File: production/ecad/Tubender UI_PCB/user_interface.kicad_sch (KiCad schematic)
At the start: 17 parts, among them IC3 SN74LVC1G29DCTR, J1 640387-5, J2 1-640387-0, J3 104031-0811, J4 640387-5, U5 74HC595, U6 PEC11R-4215K-S0024

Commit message: Added Display Daughter Board PCB and start UI layout
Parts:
- added C1: 0.1u, Capacitor_SMD:C_0805_2012Metric, symbol Device:C_Small
- added J5, J6: 4-1734592-0, footprints:TE_4-1734592-0, symbol SamacSys_Parts:4-1734592-0
- IC3: footprint footprints:SOP65P780X200-28N -> footprints:DCT0008A_N
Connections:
- net +3V3: now also C1.1, J5.4, J6.4; no longer C10.2, C11.2, C18.2, IC3.4 (GND), J1.5, J2.10, J3.6 (VSS), J4.5, U5.8 (GND), U6.5 (C)
- new net +24V: J5.2, J6.2
- new net BLUE0: J5.24, J6.24
- new net BLUE1: J5.25, J6.25
- new net BLUE2: J5.26, J6.26
- new net BLUE3: J5.27, J6.27
- new net BLUE4: J5.28, J6.28
- new net DE: J5.34, J6.34
- new net GND: C1.2, C10.2, C11.2, C18.2, IC3.4 (GND), J1.5, J2.10, J3.6 (VSS), J4.5, J5.13, J5.14, J5.21, J5.22, J5.23, J5.29, J5.3, J5.36, J5.5, J5.6, J5.7, J6.13, J6.14, J6.21, J6.22, J6.23, J6.29, J6.3, J6.36, J6.5, J6.6, J6.7, U5.8 (GND), U6.5 (C)
- new net GREEN0: J5.15, J6.15
- new net GREEN1: J5.16, J6.16
- new net GREEN2: J5.17, J6.17
- new net GREEN3: J5.18, J6.18
- new net GREEN4: J5.19, J6.19
- new net GREEN5: J5.20, J6.20
- new net HSYNC: J5.32, J6.32
- new net LEDK: J5.1, J6.1
- new net ON/OFF: J5.31, J6.31
- new net PIXCLK: J5.30, J6.30
- new net RED0: J5.8, J6.8
- new net RED1: J5.9, J6.9
- new net RED2: J5.10, J6.10
- new net RED3: J5.11, J6.11
- new net RED4: J5.12, J6.12
- new net TOUCH_XN: J5.39, J6.39
- new net TOUCH_XP: J5.37, J6.37
- new net TOUCH_YN: J5.38, J6.38
- new net TOUCH_YP: J5.40, J6.40
- new net VSYNC: J5.33, J6.33
- no-connect marks 6 -> 8
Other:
- note added: "Display Connectors"
- moved on the sheet: C10, C11, C18, DS1, IC3, J1, J2, J3, J4, R20, R22, TP1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

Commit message: Finished First Draft Layout of UI PCB
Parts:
- removed J5, J6: 4-1734592-0, footprints:TE_4-1734592-0, symbol SamacSys_Parts:4-1734592-0
- IC3: footprint footprints:DCT0008A_N -> footprints:SOP65P400X130-8N
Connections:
- net +5V: now also J2.10; no longer J2.1
- net GND: now also J2.1; no longer J2.10
- no-connect marks 8 -> 6
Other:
- note removed: "Display Connectors"
- moved on the sheet: C1, C10, C11, C18, DS1, IC3, J1, J2, J3, J4, R20, R22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

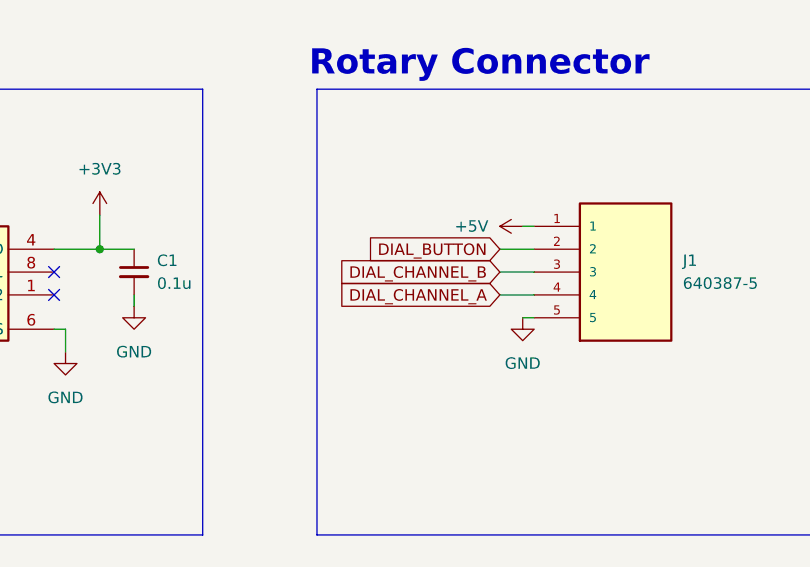
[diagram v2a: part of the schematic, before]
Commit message: Fixed DRC issues with UI board and added mounting holes
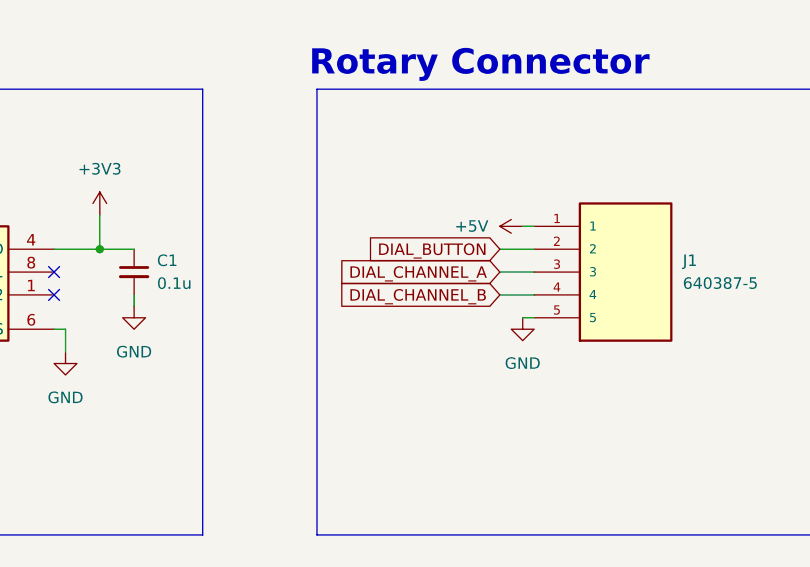
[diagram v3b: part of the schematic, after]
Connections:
- net DIAL_CHANNEL_A: now also J1.3; no longer J1.4
- net DIAL_CHANNEL_B: now also J1.4; no longer J1.3
